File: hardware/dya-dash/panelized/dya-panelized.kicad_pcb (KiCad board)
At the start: 2 copper layers, 187.9 x 127.2 mm, 276 parts, among them J1 Conn_01x06_Pin, P2_C1 100nF, P2_C3 10uF X7R, P2_C4 10nF X7R, P2_C5 100nF X7R, P2_C6 10nF, P2_C7 10uF, P2_C8 100nF, P2_J1 Conn_01x06_Pin, P2_R1 51kΩ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

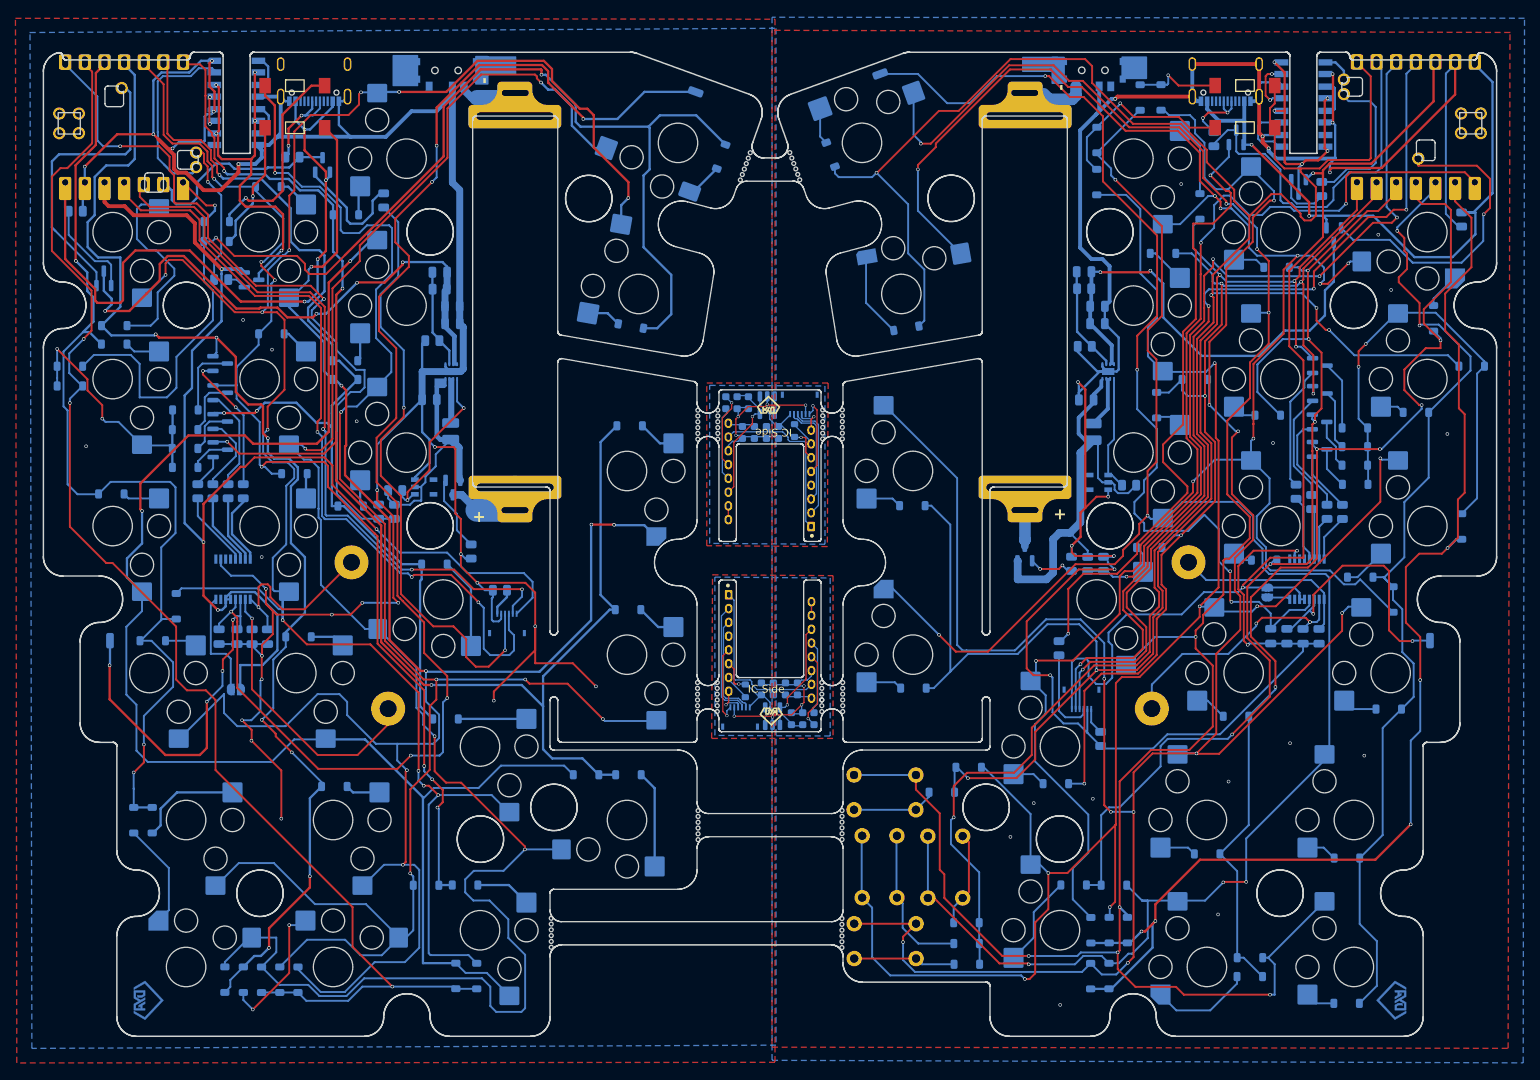
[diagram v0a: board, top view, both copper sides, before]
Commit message: Change FFC connector direction for arrow model
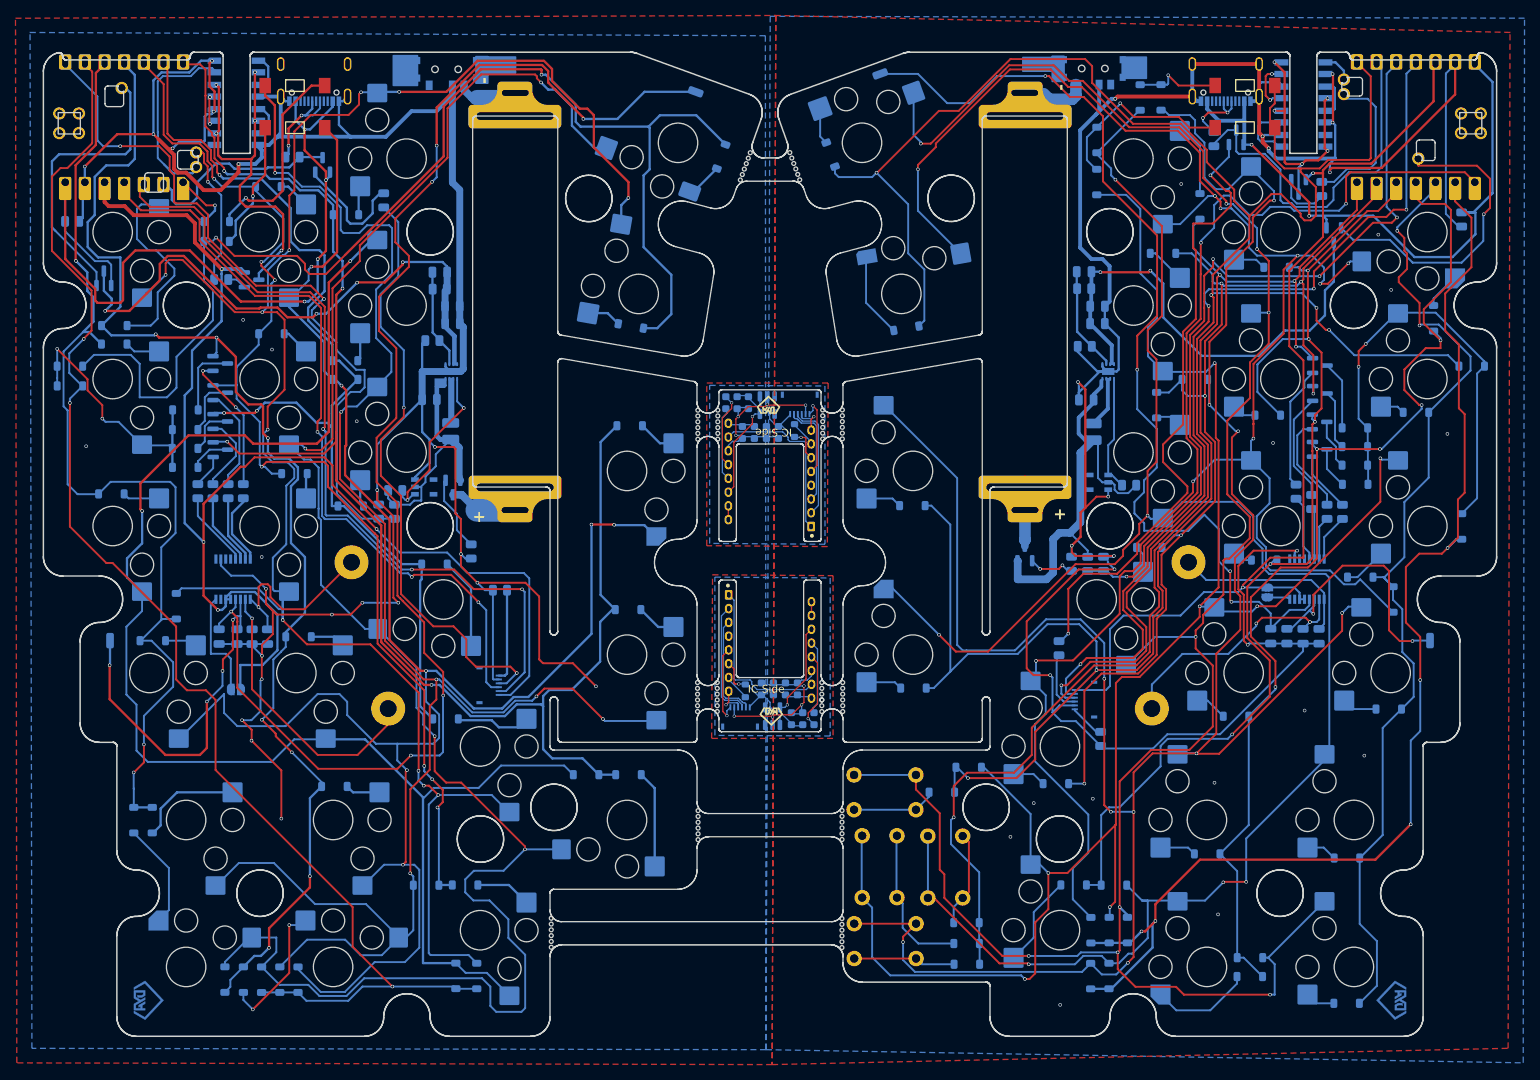
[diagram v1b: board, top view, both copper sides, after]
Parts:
- moved ? 225.0 mm to (110.7, 21.5)
- moved JL3 9.30 mm to (89.9, 112.6), turned to 90 degrees
- moved JR3 1.49 mm to (164.3, 114.4), turned to -90 degrees
- moved RL12 1.39 mm to (34.7, 52.6)
- moved SW_BATR1 0.23 mm to (166.7, 32.8)
- moved SW_BATL1 0.15 mm to (83.1, 32.9)
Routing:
- net 3.3V_L: track 161.3 -> 173.3 mm
- net SCLK_L: track 93.7 -> 105.3 mm
- net 3.3V_R: track 136.9 -> 128.3 mm
- net Net-(JL3-Pin_6): track 3.56 -> 11.9 mm
- net Net-(DL28-A): track 237.2 -> 242.2 mm
- net GNDL: track 683.3 -> 679.4 mm, vias 54 -> 52
- net MOTION_R: track 11.5 -> 7.93 mm
- net SDIO_L: track 102.8 -> 99.7 mm
- net PINL5: track 194.2 -> 197.0 mm
- net Net-(DL21-A): track 216.7 -> 219.2 mm
- net SDIO_R: track 118.6 -> 120.0 mm
- net Net-(JR3-Pin_6): track 3.46 -> 4.63 mm
- net Net-(DL25-K): track 8.82 -> 9.72 mm
- net MOTION_L: track 79.6 -> 78.7 mm
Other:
- outline, holes or cut-outs redrawn
- board text added: "${REFERENCE}"
- board text added: "DYA Dash Rev2.2"
- board text removed: "DYA Dash Rev2.1"
